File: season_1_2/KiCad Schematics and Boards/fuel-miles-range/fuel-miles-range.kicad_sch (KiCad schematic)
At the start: 0 parts

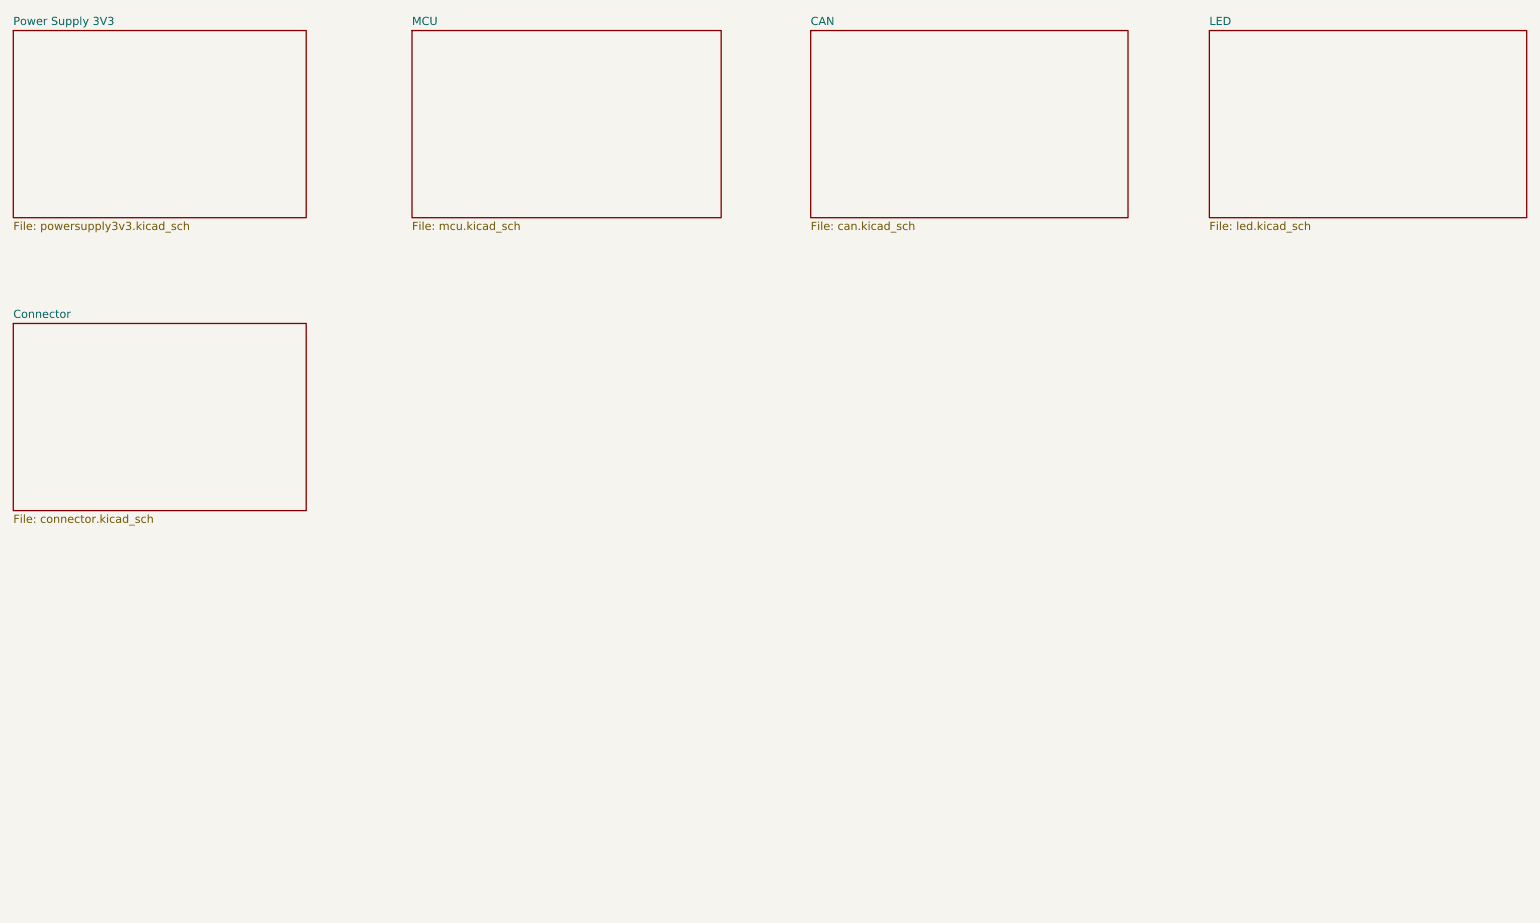
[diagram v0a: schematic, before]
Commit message: Added lots of electronic devices and routes
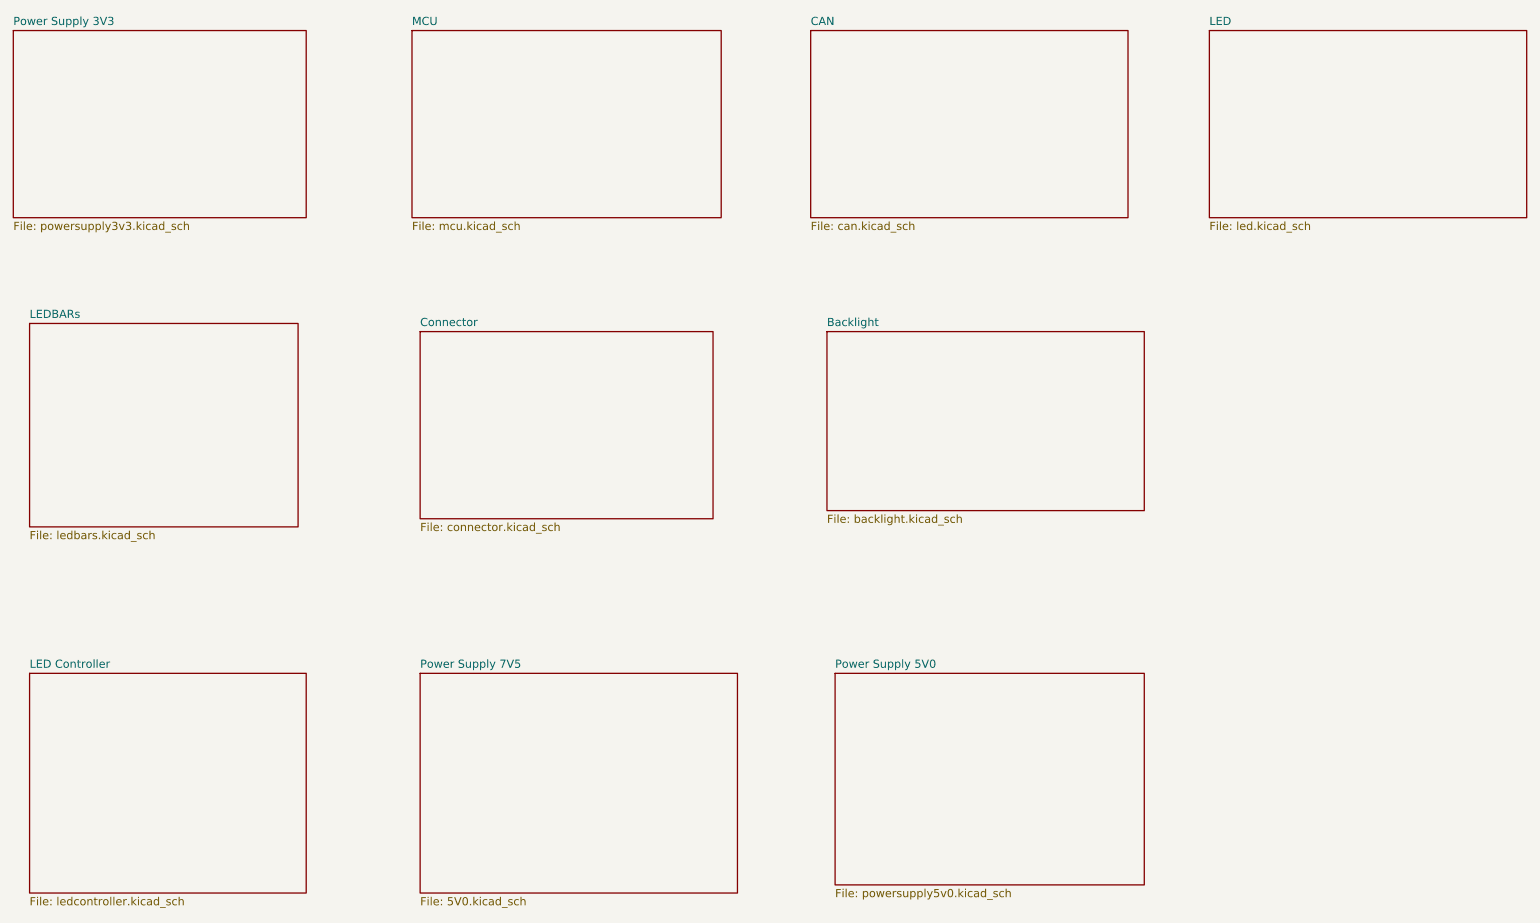
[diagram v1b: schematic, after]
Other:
- added sheet Backlight (backlight.kicad_sch)
- added sheet LED Controller (ledcontroller.kicad_sch)
- added sheet LEDBARs (ledbars.kicad_sch)
- added sheet Power Supply 5V0 (powersupply5v0.kicad_sch)
- added sheet Power Supply 7V5 (5V0.kicad_sch)
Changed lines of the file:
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@@
 			(project "fuel-miles-range"
 				(path "/431d18a8-5a30-4abd-b179-1e9443c4ac96"
-					(page "5")
+					(page "7")
+				)
+			)
+		)
+	)
+	(sheet
+		(at 24.13 67.31)
+		(size 41.91 31.75)
+		(exclude_from_sim no)
+		(in_bom yes)
+		(on_board yes)
+		(dnp no)
+		(fields_autoplaced yes)
+		(stroke
+			(width 0.1524)
+			(type solid)
+		)
+		(fill
+			(color 0 0 0 0.0000)
+		)
+		(property "Sheetname" "LEDBARs"
+			(at 24.13 66.5984 0)
+			(effects
+				(font
+					(size 1.27 1.27)
+				)
+				(justify left bottom)
+			)
+		)
+		(property "Sheetfile" "ledbars.kicad_sch"
+			(at 24.13 99.6446 0)
+			(effects
+				(font
+					(size 1.27 1.27)
+				)
+				(justify left top)
+			)
+		)
+		(instances
+			(project "fuel-miles-range"
+				(path "/431d18a8-5a30-4abd-b179-1e9443c4ac96"
+					(page "8")
 				)
 			)
@@
 			(project "fuel-miles-range"
 				(path "/431d18a8-5a30-4abd-b179-1e9443c4ac96"
+					(page "5")
+				)
+			)
+		)
+	)
+	(sheet
+		(at 149.86 121.92)
+		(size 48.26 33.02)
+		(exclude_from_sim no)
+		(in_bom yes)
+		(on_board yes)
+		(dnp no)
+		(fields_autoplaced yes)
+		(stroke
+			(width 0.1524)
+			(type solid)
+		)
+		(fill
+			(color 0 0 0 0.0000)
+		)
+		(property "Sheetname" "Power Supply 5V0"
+			(at 149.86 121.2084 0)
+			(effects
+				(font
+					(size 1.27 1.27)
+				)
+				(justify left bottom)
+			)
+		)
+		(property "Sheetfile" "powersupply5v0.kicad_sch"
+			(at 149.86 155.5246 0)
+			(effects
+				(font
+					(size 1.27 1.27)
+				)
+				(justify left top)
+			)
+		)
+		(instances
+			(project "fuel-miles-range"
+				(path "/431d18a8-5a30-4abd-b179-1e9443c4ac96"
 					(page "3")
+				)
+			)
+		)
+	)
+	(sheet
+		(at 85.09 121.92)
+		(size 49.53 34.29)
+		(exclude_from_sim no)
+		(in_bom yes)
+		(on_board yes)
+		(dnp no)
+		(fields_autoplaced yes)
+		(stroke
+			(width 0.1524)
+			(type solid)
+		)
+		(fill
+			(color 0 0 0 0.0000)
+		)
+		(property "Sheetname" "Power Supply 7V5"
+			(at 85.09 121.2084 0)
+			(effects
+				(font
+					(size 1.27 1.27)
+				)
+				(justify left bottom)
+			)
+		)
+		(property "Sheetfile" "5V0.kicad_sch"
+			(at 85.09 156.7946 0)
+			(effects
+				(font
+					(size 1.27 1.27)
+				)
+				(justify left top)
+			)
+		)
+		(instances
+			(project "fuel-miles-range"
+				(path "/431d18a8-5a30-4abd-b179-1e9443c4ac96"
+					(page "4")
 				)
 			)
@@
 			(project "fuel-miles-range"
 				(path "/431d18a8-5a30-4abd-b179-1e9443c4ac96"
-					(page "4")
-				)
-			)
-		)
-	)
-	(sheet
-		(at 21.59 67.31)
+					(page "6")
+				)
+			)
+		)
+	)
+	(sheet
+		(at 85.09 68.58)
 		(size 45.72 29.21)
 		(exclude_from_sim no)
@@
 		)
 		(property "Sheetname" "Connector"
-			(at 21.59 66.5984 0)
+			(at 85.09 67.8684 0)
 			(effects
 				(font
@@
 		)
 		(property "Sheetfile" "connector.kicad_sch"
-			(at 21.59 97.1046 0)
-			(effects
-				(font
-					(size 1.27 1.27)
-				)
-				(justify left top)
-			)
-		)
-		(instances
-			(project "fuel-miles-range"
-				(path "/431d18a8-5a30-4abd-b179-1e9443c4ac96"
-					(page "6")
+			(at 85.09 98.3746 0)
+			(effects
+				(font
+					(size 1.27 1.27)
+				)
+				(justify left top)
+			)
+		)
+		(instances
+			(project "fuel-miles-range"
+				(path "/431d18a8-5a30-4abd-b179-1e9443c4ac96"
+					(page "10")
 				)
 			)
@@
 				)
 			)
+		)
+	)
+	(sheet
+		(at 24.13 121.92)
+		(size 43.18 34.29)
+		(exclude_from_sim no)
+		(in_bom yes)
+		(on_board yes)
+		(dnp no)
+		(fields_autoplaced yes)
+		(stroke
+			(width 0.1524)
+			(type solid)
+		)
+		(fill
+			(color 0 0 0 0.0000)
+		)
+		(property "Sheetname" "LED Controller"
+			(at 24.13 121.2084 0)
+			(effects
+				(font
+					(size 1.27 1.27)
+				)
+				(justify left bottom)
+			)
+		)
+		(property "Sheetfile" "ledcontroller.kicad_sch"
+			(at 24.13 156.7946 0)
+			(effects
+				(font
+					(size 1.27 1.27)
+				)
+				(justify left top)
+			)
+		)
+		(instances
+			(project "fuel-miles-range"
+				(path "/431d18a8-5a30-4abd-b179-1e9443c4ac96"
+					(page "9")
+				)
+			)
+		)
+	)
+	(sheet
+		(at 148.59 68.58)
+		(size 49.53 27.94)
+		(exclude_from_sim no)
+		(in_bom yes)
+		(on_board yes)
+		(dnp no)
+		(fields_autoplaced yes)
+		(stroke
+			(width 0.1524)
+			(type solid)
+		)
+		(fill
+			(color 0 0 0 0.0000)
+		)
+		(property "Sheetname" "Backlight"
+			(at 148.59 67.8684 0)
+			(effects
+				(font
+					(size 1.27 1.27)
+				)
+				(justify left bottom)
+			)
+		)
+		(property "Sheetfile" "backlight.kicad_sch"
+			(at 148.59 97.1046 0)
+			(effects
+				(font
+					(size 1.27 1.27)
+				)
+				(justify left top)
+			)
+		)
+		(instances
+			(project "fuel-miles-range"
+				(path "/431d18a8-5a30-4abd-b179-1e9443c4ac96"
+					(page "11")
+				)
+			)
